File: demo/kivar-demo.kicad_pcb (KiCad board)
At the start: 2 copper layers, 57 x 36 mm, 60 parts, among them U1 24C02, U2 MIC841HYC5, U3 ISL91127IRAZ, U4 TCA9535PWR, U6 AP3032

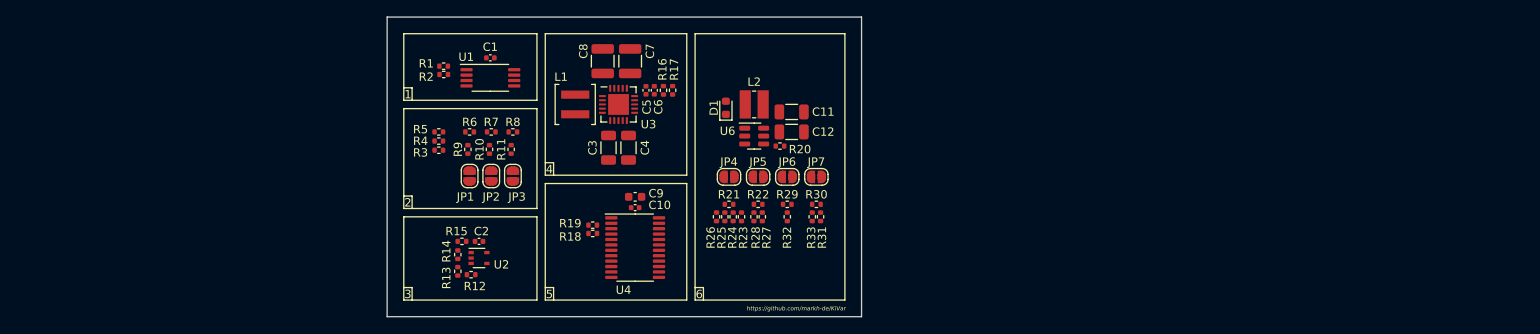
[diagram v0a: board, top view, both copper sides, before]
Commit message: For each aspect, add a "VarID" field in an essential component to create a board variant ID code
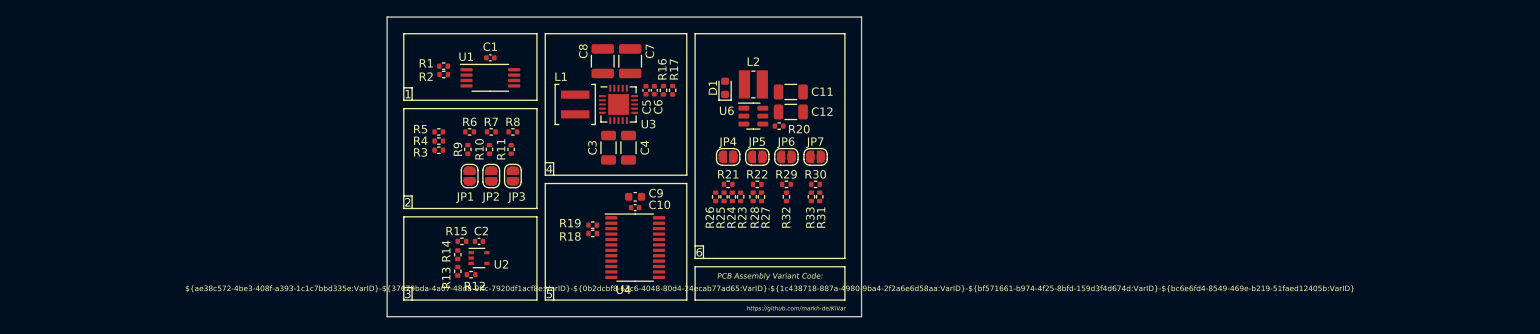
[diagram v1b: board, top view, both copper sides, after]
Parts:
- moved D1 2.40 mm to (94.6, 85.5)
- moved JP4 2.40 mm to (95.0, 93.8)
- moved JP5 2.40 mm to (98.5, 93.8)
- moved JP6 2.40 mm to (102.0, 93.8)
- moved JP7 2.40 mm to (105.5, 93.8)
- moved R20 2.40 mm to (101.1, 90.1)
- moved R21 2.40 mm to (95.0, 97.1)
- moved R22 2.40 mm to (98.5, 97.1)
- moved R23 2.40 mm to (96.5, 98.6)
- moved R24 2.40 mm to (95.5, 98.6)
- moved R25 2.40 mm to (94.5, 98.6)
- moved R26 2.40 mm to (93.5, 98.6)
- moved R27 2.40 mm to (99.0, 98.6)
- moved R28 2.40 mm to (98.0, 98.6)
- moved R29 2.40 mm to (102.0, 97.1)
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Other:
- board text added: "${ae38c572-4be3-408f-a393-1c1c7bbd335e:VarID}-${37679bda-4a07-48d8-9ffc-7920df1acf8e:VarID}-${0b2dcbf8-63c6-4048-80d4-24ecab77ad65:VarID}-${1c438718-887a-4980-9ba4-2f2a6e6d58aa:VarID}-${bf571661-b974-4f25-8bfd-159d3f4d674d:VarID}-${bc6e6fd4-8549-469e-b219-51faed12405b:VarID}"
- board text added: "PCB Assembly Variant Code:"
